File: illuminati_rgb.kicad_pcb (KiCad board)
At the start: 2 copper layers, 69 x 42 mm, 48 parts, among them IC1 TPS564247DRLR, IC2 SPH0645LM4H-1-8, J1 Conn_02x03_Odd_Even, J2 Conn_01x04, J3 Conn_01x02, J6 Conn_01x02, J7 Conn_01x04, J8 Conn_01x04, Q1 C351406, Q2 C351406, Q3 C351406, Q4 C351406, Q5 C351406, Q6 C351406, Q7 C351406, Q8 C351406, Q9 C351406, SW1 SW_SPST, U1 ESP32-WROOM-32

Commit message: v2 board
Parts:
- removed the C5 at (139.5, 87.8)
- removed IC2: SPH0645LM4H-1-8, SamacSys_Parts:SPH0645LM4H18
- removed the J2 at (185.0, 121.0)
- removed J8: Conn_01x04, TerminalBlock_Phoenix:TerminalBlock_Phoenix_MKDS-1,5-4_1x04_P5.00mm_Horizontal
- removed Q1, Q2, Q3, Q4, Q5, Q6, Q7, Q8, Q9: C351406, Package_TO_SOT_SMD:SOT-23
- removed R10, R9: 10k, Resistor_SMD:R_0805_2012Metric
- removed R11: 100k, Resistor_SMD:R_0603_1608Metric_Pad0.98x0.95mm_HandSolder
- removed R12: 22k, Resistor_SMD:R_0603_1608Metric_Pad0.98x0.95mm_HandSolder
- removed R13: NC, Resistor_SMD:R_0805_2012Metric
- removed R14: 0R, Resistor_SMD:R_0805_2012Metric
- removed R15: 10k, Resistor_SMD:R_0402_1005Metric
- removed R16: 20k, Resistor_SMD:R_0402_1005Metric
- removed the R6 at (152.5, 108.0)
- removed SW1: SW_SPST, Button_Switch_THT:SW_PUSH_6mm_H5mm
- added C1: 10u/1206, Capacitor_SMD:C_1206_3216Metric, F.Cu at (142.1, 78.8)
- added C11: 22u, Capacitor_SMD:C_0805_2012Metric, F.Cu at (121.2, 97.2)
- added C12: 22u, Capacitor_SMD:C_0805_2012Metric, F.Cu at (150.4, 114.4)
- added C13: 22u, Capacitor_SMD:C_0805_2012Metric, F.Cu at (177.8, 111.2)
- added C8: 22u, Capacitor_SMD:C_0805_2012Metric, F.Cu at (159.0, 82.6)
- added D1: B340A, Diode_SMD:D_SMA, F.Cu at (132.1, 78.8)
- added G***: LOGO, LOGO, B.Cu at (137.5, 108.0)
- added IC11: SI4174DY-T1-GE3, SamacSys_Parts:SOIC127P600X175-8N, F.Cu at (102.0, 105.5)
- added IC12: SI4174DY-T1-GE3, SamacSys_Parts:SOIC127P600X175-8N, F.Cu at (102.0, 112.5)
- added IC13: SI4174DY-T1-GE3, SamacSys_Parts:SOIC127P600X175-8N, F.Cu at (102.0, 119.5)
- added IC17: SI4174DY-T1-GE3, SamacSys_Parts:SOIC127P600X175-8N, F.Cu at (116.5, 122.0)
- added IC18: SI4174DY-T1-GE3, SamacSys_Parts:SOIC127P600X175-8N, F.Cu at (123.5, 122.0)
- added IC19: SI4174DY-T1-GE3, SamacSys_Parts:SOIC127P600X175-8N, F.Cu at (130.5, 122.0)
- added IC23: SI4174DY-T1-GE3, SamacSys_Parts:SOIC127P600X175-8N, F.Cu at (143.5, 122.0)
- added IC24: SI4174DY-T1-GE3, SamacSys_Parts:SOIC127P600X175-8N, F.Cu at (150.5, 122.0)
- added IC25: SI4174DY-T1-GE3, SamacSys_Parts:SOIC127P600X175-8N, F.Cu at (157.5, 122.0)
- added IC29: SI4174DY-T1-GE3, SamacSys_Parts:SOIC127P600X175-8N, F.Cu at (170.5, 122.0)
- added IC30: SI4174DY-T1-GE3, SamacSys_Parts:SOIC127P600X175-8N, F.Cu at (177.5, 122.0)
- added IC31: SI4174DY-T1-GE3, SamacSys_Parts:SOIC127P600X175-8N, F.Cu at (184.5, 122.0)
- added IC5: SI4174DY-T1-GE3, SamacSys_Parts:SOIC127P600X175-8N, F.Cu at (102.0, 78.5)
- added IC6: SI4174DY-T1-GE3, SamacSys_Parts:SOIC127P600X175-8N, F.Cu at (102.0, 85.5)
- added IC7: SI4174DY-T1-GE3, SamacSys_Parts:SOIC127P600X175-8N, F.Cu at (102.0, 92.5)
- added J1: Conn_01x04, TerminalBlock_Phoenix:TerminalBlock_Phoenix_MKDS-1,5-4_1x04_P5.00mm_Horizontal, F.Cu at (89.0, 133.0)
- added J4: Conn_01x04, TerminalBlock_Phoenix:TerminalBlock_Phoenix_MKDS-1,5-4_1x04_P5.00mm_Horizontal, F.Cu at (91.0, 105.0)
- added J5: Conn_01x04, TerminalBlock_Phoenix:TerminalBlock_Phoenix_MKDS-1,5-4_1x04_P5.00mm_Horizontal, F.Cu at (116.0, 133.0)
- added JP1: Jumper_2_Bridged, Jumper:SolderJumper-2_P1.3mm_Bridged_RoundedPad1.0x1.5mm, F.Cu at (182.0, 101.0)
- added JP2: Jumper_2_Bridged, Jumper:SolderJumper-2_P1.3mm_Bridged_RoundedPad1.0x1.5mm, F.Cu at (179.2, 101.0)
- added JP3: Jumper_2_Bridged, Jumper:SolderJumper-2_P1.3mm_Bridged_RoundedPad1.0x1.5mm, F.Cu at (161.9, 96.6)
- added JP4: Jumper_2_Bridged, Jumper:SolderJumper-2_P1.3mm_Bridged_RoundedPad1.0x1.5mm, F.Cu at (188.0, 101.0)
- added JP5: Jumper_2_Bridged, Jumper:SolderJumper-2_P1.3mm_Bridged_RoundedPad1.0x1.5mm, F.Cu at (161.9, 93.8)
- added PS1: AP5100WG-7, SamacSys_Parts:SOT95P285X140-6N, F.Cu at (136.1, 80.3)
- added R1: 10k, Resistor_SMD:R_0603_1608Metric, F.Cu at (164.7, 94.1)
- added U2: 74HC14, Package_SO:SOIC-14_3.9x8.7mm_P1.27mm, F.Cu at (114.2, 94.6)
- added U3: 74HC14, Package_SO:SOIC-14_3.9x8.7mm_P1.27mm, F.Cu at (143.6, 112.0)
- added U4: 74HC14, Package_SO:SOIC-14_3.9x8.7mm_P1.27mm, F.Cu at (183.6, 111.2)
- C10: renamed from C8; value 10u -> 22u; footprint Capacitor_SMD:C_0805_2012Metric_Pad1.18x1.45mm_HandSolder -> Capacitor_SMD:C_0805_2012Metric
- C2: value 22u -> 10u/1206; footprint Capacitor_SMD:C_0805_2012Metric -> Capacitor_SMD:C_1206_3216Metric
- C3: value 100n -> 22n; footprint Capacitor_SMD:C_0603_1608Metric_Pad1.08x0.95mm_HandSolder -> Capacitor_SMD:C_0603_1608Metric
- C4, C9: value 100n -> 22u; footprint Capacitor_SMD:C_0603_1608Metric_Pad1.08x0.95mm_HandSolder -> Capacitor_SMD:C_0805_2012Metric
- C5: renamed from C1; footprint Capacitor_SMD:C_0805_2012Metric_Pad1.18x1.45mm_HandSolder -> Capacitor_SMD:C_0603_1608Metric
- C7: value 56p -> 100p; footprint Capacitor_SMD:C_0603_1608Metric_Pad1.08x0.95mm_HandSolder -> Capacitor_SMD:C_0603_1608Metric
- G***, J7: moved to F.Cu
- IC1: value TPS564247DRLR -> ESP32-C3-WROOM-02-N4; footprint SamacSys_Parts:SOT50P160X60-6N -> SamacSys_Parts:ESP32C3WROOM02N4
- J2: renamed from J1; moved to F.Cu
- J3, J6: value Conn_01x02 -> Conn_01x04; footprint TerminalBlock_Phoenix:TerminalBlock_Phoenix_MKDS-1,5-2_1x02_P5.00mm_Horizontal -> TerminalBlock_Phoenix:TerminalBlock_Phoenix_MKDS-1,5-4_1x04_P5.00mm_Horizontal; moved to F.Cu
- L1: value 1.5u -> 10u/C2921170; footprint Inductor_SMD:L_Wuerth_MAPI-4020 -> Inductor_SMD:L_Chilisin_BMRA00040420
- R2, R3, R4, R7: footprint Resistor_SMD:R_0805_2012Metric -> Resistor_SMD:R_0603_1608Metric
- R5, R8: value 10k -> 2k; footprint Resistor_SMD:R_0805_2012Metric -> Resistor_SMD:R_0603_1608Metric
- R6: renamed from R1; footprint Resistor_SMD:R_0805_2012Metric -> Resistor_SMD:R_0603_1608Metric
- U1: value ESP32-WROOM-32 -> AMS1117-3.3; footprint RF_Module:ESP32-WROOM-32 -> Package_TO_SOT_SMD:SOT-223-3_TabPin2
- moved J6 60.9 mm to (143.0, 133.0), turned to 0 degrees
- moved R8 50.2 mm to (135.8, 84.3), turned to -90 degrees
- moved R5 44.4 mm to (137.4, 84.3), turned to 90 degrees
- moved IC1 43.0 mm to (179.5, 91.0), turned to 0 degrees
- moved J3 38.1 mm to (91.0, 78.0), turned to -90 degrees
- moved R4 27.6 mm to (139.1, 84.3), turned to -90 degrees
- moved R7 24.1 mm to (134.2, 84.3), turned to 90 degrees
- moved J2 23.7 mm to (170.5, 103.5)
- moved R3 23.4 mm to (166.3, 94.1), turned to -90 degrees
- moved R6 22.7 mm to (165.8, 87.5), turned to -90 degrees
- moved C10 21.5 mm to (164.8, 84.8)
- moved H1 21.2 mm to (119.0, 104.0)
- moved C5 20.9 mm to (164.2, 87.5), turned to 90 degrees
- moved L1 20.0 mm to (127.1, 76.1)
- moved G*** 19.0 mm to (137.5, 100.0), turned to 0 degrees
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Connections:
- C3 pad 1: VCC -> Net-(PS1-BST)
- C3 pad 2: GND -> Net-(D1-K)
- C4 pad 1: +3V3 -> +5V
- C6 pad 1: +3V3 -> +5V
- C7 pad 1: +3V3 -> +5V
- C7 pad 2: Net-(IC1-FB) -> /V_FB
- C9 pad 1: GND -> +3V3
- C9 pad 2: +3V3 -> GND
- IC1 pad 1: VCC -> +3V3
- IC1 pad 2: Net-(IC1-SW) -> /esp_en
- IC1 pad 3: GND -> /R1
- IC1 pad 4: GND -> /G1
- IC1 pad 5: Net-(IC1-EN) -> /B1
- IC1 pad 6: Net-(IC1-FB) -> /R2
- J3 pad 2: GND -> /RGB Channel1/OUT_R
- J6 pad 2: GND -> /RGB Channel4/OUT_R
- J7 pad 2: /B2_OUT -> /RGB Channel5/OUT_R
- J7 pad 3: /G2_OUT -> /RGB Channel5/OUT_G
- J7 pad 4: /R2_OUT -> /RGB Channel5/OUT_B
- L1 pad 1: +3V3 -> Net-(D1-K)
- L1 pad 2: Net-(IC1-SW) -> +5V
- R2 pad 1: /R1 -> +3V3
- R2 pad 2: GND -> /gpio2
- R3 pad 1: /R2 -> +3V3
- R3 pad 2: GND -> /boot
- R4 pad 1: /R3 -> Net-(PS1-EN)
- R4 pad 2: GND -> VCC
- R5 pad 1: /G1 -> GND
- R5 pad 2: GND -> Net-(PS1-EN)
- R7 pad 1: /G3 -> +5V
- R7 pad 2: GND -> /V_FB
- R8 pad 1: /B1 -> /V_FB
- U1 pad 3: /esp_en -> +5V
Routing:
- net +5V: track 0.00 -> 242.0 mm, vias 0 -> 6
- net /B4: track 0.00 -> 53.2 mm
- net /R4: track 0.00 -> 46.6 mm
- net /G4: track 0.00 -> 46.4 mm
- net /R2: track 18.7 -> 61.3 mm
- net VCC: track 25.8 -> 67.4 mm
- net /G5: track 0.00 -> 35.1 mm
- net /B5: track 0.00 -> 34.9 mm
- net /B2: track 14.6 -> 48.4 mm
- net /RGB Channel3/R: track 0.00 -> 32.3 mm
- net /G1: track 25.4 -> 57.4 mm
- net /B3: track 22.2 -> 52.9 mm
- net /B1: track 29.7 -> 59.9 mm
- net /G2: track 20.5 -> 50.2 mm
- net /G3: track 26.9 -> 56.2 mm
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- added copper zone on F.Cu, net /RGB Channel1/OUT_B
- added copper zone on F.Cu, net /RGB Channel1/OUT_G
- added copper zone on F.Cu, net /RGB Channel1/OUT_R
- added copper zone on F.Cu, net /RGB Channel2/OUT_B
- added copper zone on F.Cu, net /RGB Channel2/OUT_G
- added copper zone on F.Cu, net /RGB Channel2/OUT_R
- added copper zone on F.Cu, net /RGB Channel3/OUT_B
- added copper zone on F.Cu, net /RGB Channel3/OUT_G
- added copper zone on F.Cu, net /RGB Channel3/OUT_R
- added copper zone on F.Cu, net /RGB Channel4/OUT_B
- added copper zone on F.Cu, net /RGB Channel4/OUT_G
- added copper zone on F.Cu, net /RGB Channel4/OUT_R
- added copper zone on F.Cu, net /RGB Channel5/OUT_B
- added copper zone on F.Cu, net /RGB Channel5/OUT_G
- added copper zone on F.Cu, net /RGB Channel5/OUT_R
- added copper zone on F.Cu, net Net-(D1-K)
- removed copper zone on F.Cu, net +3V3
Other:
- board size 69 x 42 mm -> 108 x 69 mm
- board text added: "3.3v"
- board text added: "B0"
- board text added: "B18"
- board text added: "B21"
- board text added: "B6"
- board text added: "B9"
- board text added: "CH4"
- board text added: "CH5"
- board text added: "G1"
- board text added: "G19"
- board text added: "G20"
- board text added: "G5"
- board text added: "G8"
- board text added: "R10"
- board text added: "R2"
- board text added: "R3"
- board text added: "R4"
- board text added: "R7"
- board text added: "boot"
- board text added: "en"
- board text added: "gnd"
- board text added: "rx"
- board text added: "tx"
- board text removed: "B13"
- board text removed: "B19"
- board text removed: "B25"
- board text removed: "G18"
- board text removed: "G27"
- board text removed: "G33"
- board text removed: "R17"
- board text removed: "R26"
- board text removed: "R32"

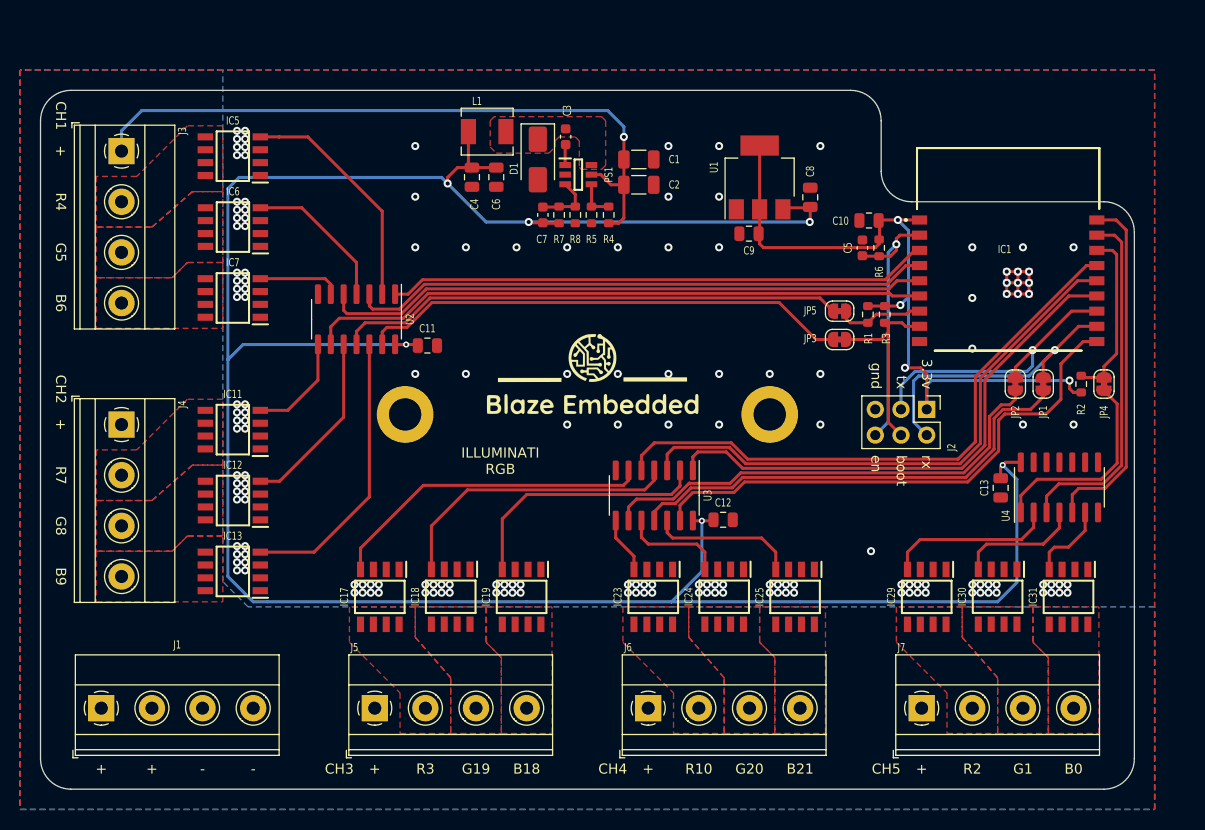
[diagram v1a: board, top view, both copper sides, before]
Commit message: V2.1 swap esp32c3 for esp32 and change form factor
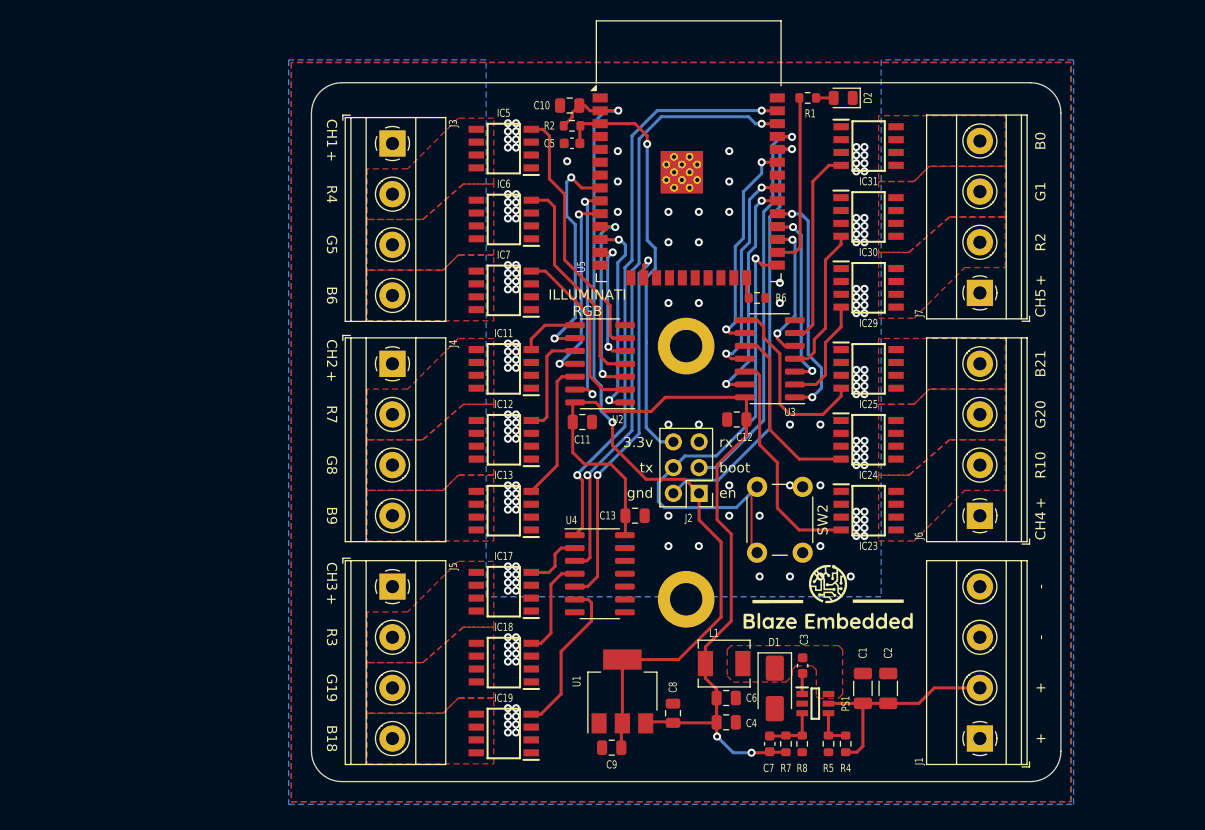
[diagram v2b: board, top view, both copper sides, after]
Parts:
- removed IC1: ESP32-C3-WROOM-02-N4, SamacSys_Parts:ESP32C3WROOM02N4
- removed JP1, JP2, JP3, JP4, JP5: Jumper_2_Bridged, Jumper:SolderJumper-2_P1.3mm_Bridged_RoundedPad1.0x1.5mm
- removed R3: 10k, Resistor_SMD:R_0603_1608Metric
- added D2: LED, LED_SMD:LED_0805_2012Metric, F.Cu at (162.2, 72.8)
- added SW2: SW_SPST, Button_Switch_THT:SW_PUSH_6mm_H8mm, F.Cu at (158.2, 111.2)
- added U5: ESP32-WROOM-32, RF_Module:ESP32-WROOM-32, F.Cu at (147.0, 81.0)
- R1: value 10k -> 2k
- moved J1 86.8 mm to (175.8, 136.0), turned to 90 degrees
- moved C4 59.4 mm to (150.7, 134.4), turned to 0 degrees
- moved L1 57.5 mm to (150.5, 128.6)
- moved C3 57.2 mm to (158.2, 128.8)
- moved D1 57.2 mm to (155.5, 131.1)
- moved PS1 57.2 mm to (159.5, 132.6)
- moved R4 57.2 mm to (162.5, 136.5)
- moved R5 57.2 mm to (160.8, 136.5)
- moved C7 56.8 mm to (155.0, 136.5)
- moved R7 56.8 mm to (156.6, 136.5)
- moved R8 56.8 mm to (158.2, 136.5)
- moved C1 56.7 mm to (164.2, 131.1), turned to 90 degrees
- moved R2 56.4 mm to (135.5, 75.5), turned to 0 degrees
- moved C6 56.2 mm to (150.7, 132.0), turned to 0 degrees
- moved C2 55.5 mm to (166.7, 131.1), turned to 90 degrees
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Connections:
- R1 pad 1: +3V3 -> Net-(U5-IO4)
- R1 pad 2: /gpio8 -> Net-(D2-A)
- R2 pad 2: /gpio2 -> /esp_en
- R6 pad 1: +3V3 -> Net-(U5-IO2)
- R6 pad 2: /esp_en -> GND
- U2 pad 1: /R1 -> /B1
- U2 pad 2: /RGB Channel1/R -> /RGB Channel1/B
- U2 pad 5: /B1 -> /R1
- U2 pad 6: /RGB Channel1/B -> /RGB Channel1/R
- U3 pad 1: /B3 -> /R5
- U3 pad 12: /RGB Channel4/B -> /RGB Channel4/R
- U3 pad 13: /B4 -> /R4
- U3 pad 2: /RGB Channel3/B -> /RGB Channel5/R
- U3 pad 3: /G3 -> /G5
- U3 pad 4: /RGB Channel3/G -> /RGB Channel5/G
- U3 pad 5: /R3 -> /B5
- U3 pad 6: /RGB Channel3/R -> /RGB Channel5/B
- U3 pad 8: /RGB Channel4/R -> /RGB Channel4/B
- U3 pad 9: /R4 -> /B4
- U4 pad 1: /R5 -> /R3
- U4 pad 2: /RGB Channel5/R -> /RGB Channel3/R
- U4 pad 3: /G5 -> /G3
- U4 pad 4: /RGB Channel5/G -> /RGB Channel3/G
- U4 pad 5: /B5 -> /B3
- U4 pad 6: /RGB Channel5/B -> /RGB Channel3/B
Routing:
- net +5V: track 242.0 -> 86.1 mm, vias 6 -> 2
- net VCC: track 67.4 -> 21.8 mm, vias 1 -> 0
- net /R1: track 53.6 -> 12.6 mm, vias 0 -> 2
- net /B1: track 59.9 -> 20.4 mm, vias 0 -> 2
- net /R2: track 61.3 -> 22.6 mm, vias 0 -> 2
- net /G1: track 57.4 -> 19.4 mm, vias 0 -> 2
- net /B4: track 53.2 -> 21.6 mm, vias 0 -> 2
- net /G2: track 50.2 -> 19.4 mm, vias 0 -> 2
- net /boot: track 19.8 -> 50.0 mm, vias 0 -> 1
- net /RGB Channel3/R: track 32.3 -> 6.00 mm
- net /B2: track 48.4 -> 22.8 mm, vias 0 -> 2
- net /G4: track 46.4 -> 21.8 mm, vias 0 -> 2
- net /R4: track 46.6 -> 22.9 mm, vias 0 -> 2
- net /B5: track 34.9 -> 14.1 mm, vias 0 -> 2
- net /RGB Channel3/G: track 29.1 -> 9.96 mm
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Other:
- board size 108 x 69 mm -> 74 x 69 mm
